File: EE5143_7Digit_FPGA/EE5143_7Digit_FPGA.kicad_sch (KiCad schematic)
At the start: 18 parts, among them J1 Conn_01x13, Q1 PN2222A, Q2 PN2222A, Q3 PN2222A, Q4 PN2222A, U1 CC56-12SRWA

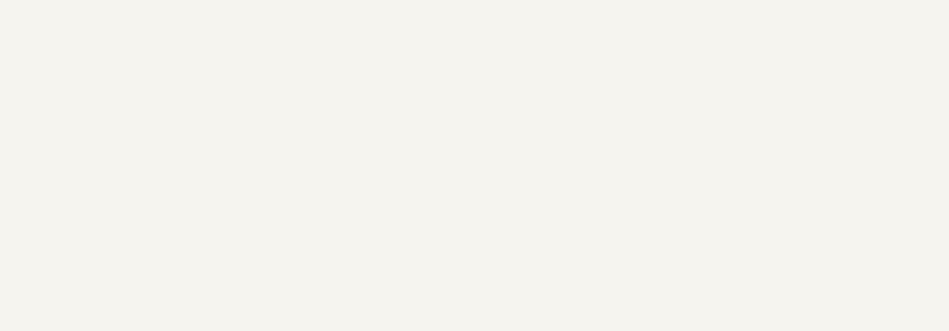
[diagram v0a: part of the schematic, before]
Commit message: Added files and updated title block of schematic
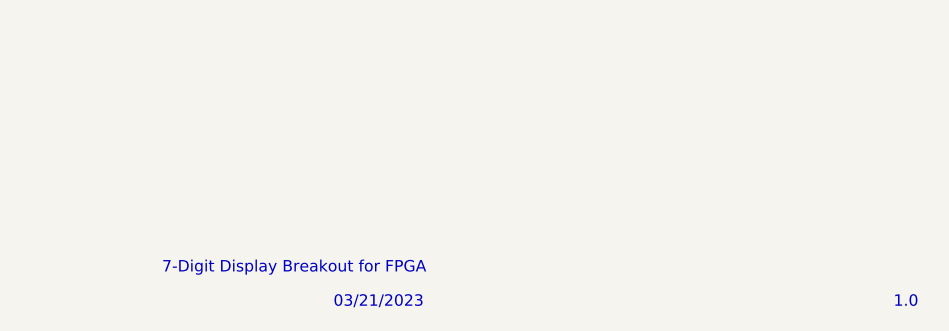
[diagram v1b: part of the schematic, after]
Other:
- note added: "03/21/2023"
- note added: "1.0"
- note added: "7-Digit Display Breakout for FPGA"
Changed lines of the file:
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@@
     (stroke (width 0) (type default))
+  )
+  (text "03/21/2023" (at 205.74 194.31 0)
+    (effects (font (size 1.27 1.27)) (justify left bottom))
+  )
+  (text "7-Digit Display Breakout for FPGA" (at 186.69 190.5 0)
+    (effects (font (size 1.27 1.27)) (justify left bottom))
+  )
+  (text "1.0" (at 267.97 194.31 0)
+    (effects (font (size 1.27 1.27)) (justify left bottom))
   )
   (global_label "G" (shape input) (at 52.07 64.77 180) (fields_autoplaced)
